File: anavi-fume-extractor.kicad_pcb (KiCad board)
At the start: 2 copper layers, 74.9 x 40.6 mm, 34 parts, among them K1 SANYOU_SRD_Form_C, P1 CONN_01X03, Q1 BC817, U1 I2C_SENS_1, U2 I2C_SENS_1, U3 I2C_SENS_1

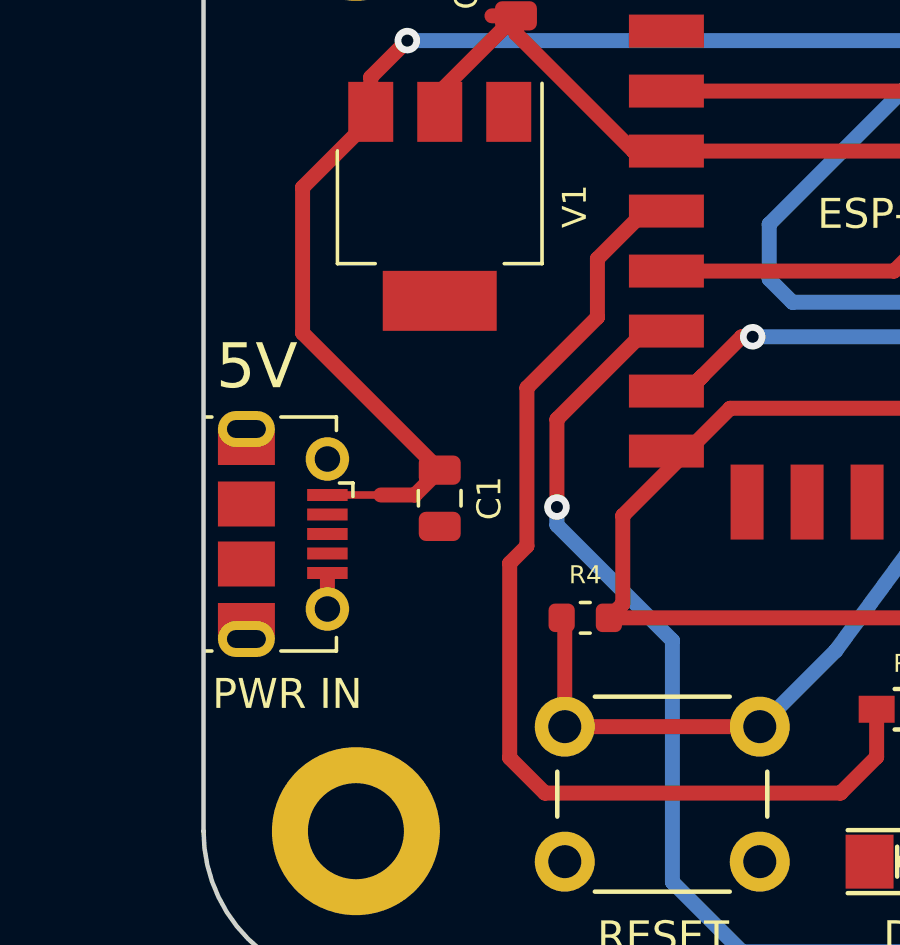
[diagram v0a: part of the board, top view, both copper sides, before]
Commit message: anavi-fume-extractor.kicad_pcb: Move capacitor
Move capacitor C1 to be closer to the microUSB connector.

Suggested-by: Rangel Ivanov <rangelivanov88@gmail.com>
Signed-off-by: Leon Anavi <leon@anavi.org>
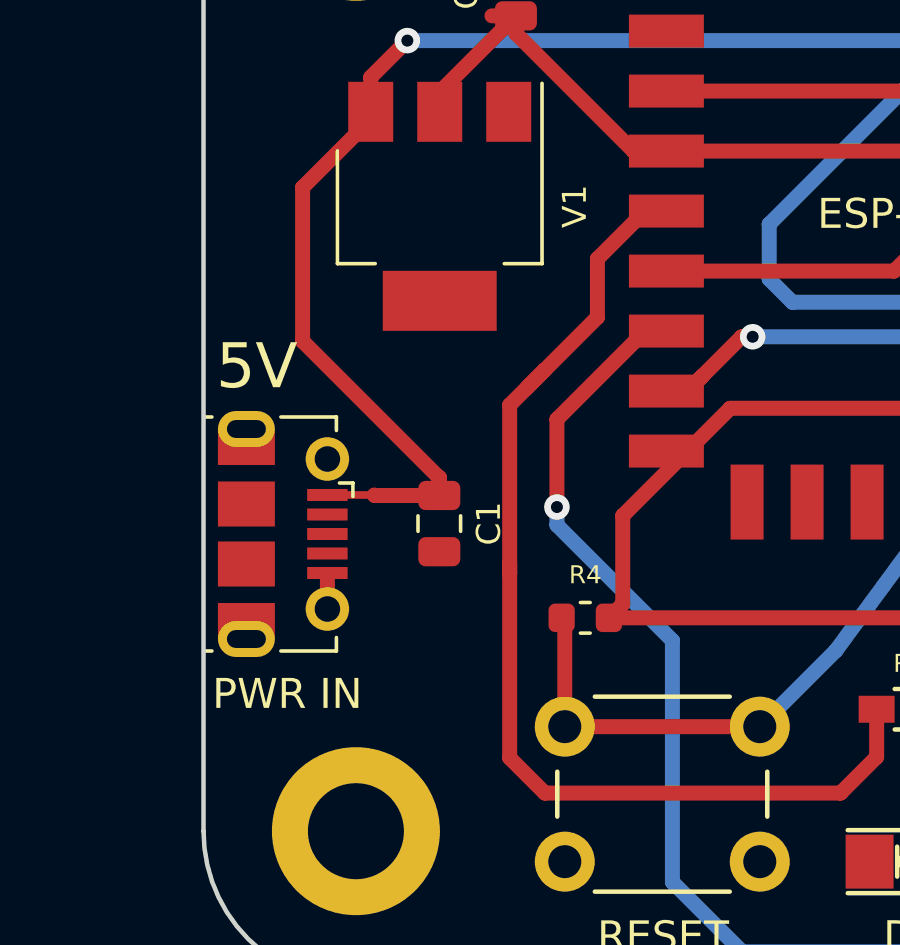
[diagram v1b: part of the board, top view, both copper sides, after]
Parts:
- moved C1 0.85 mm to (72.6, 96.4)
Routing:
- net Net-(ESP-12-Pad4): track 36.3 -> 37.5 mm
- net +5V: track 123.6 -> 124.1 mm
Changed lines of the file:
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@@
     (thickness 1.6)
     (drawings 24)
-    (tracks 235)
+    (tracks 239)
     (zones 0)
     (modules 34)
@@
   )
   (module Capacitor_SMD:C_0805_2012Metric (layer F.Cu)
-    (at 72.644 95.5825 270)
+    (at 72.63 96.4275 270)
     (descr "Capacitor SMD 0805 (2012 Metric), square (rectangular) end terminal, IPC_7351 nominal, (Body size source: https://docs.google.com/spreadsheets/d/1BsfQQcO9C6DZCsRaXUlFlo91Tg2WpOkGARC1WS5S8t0/edit?usp=sharing), generated with kicad-footprint-generator")
     (tags capacitor)
@@
       (effects (font (size 0.8 0.8) (thickness 0.15)))
     )
-    (fp_text value 10uF (at 0 -1.778 270) (layer F.Fab)
+    (fp_text value 10uF (at 2.5625 -0.14) (layer F.Fab)
       (effects (font (size 1 1) (thickness 0.15)))
     )
@@
   (segment (start 86.0044 105.41) (end 76.1492 105.41) (width 0.5) (layer F.Cu) (net 9))
   (segment (start 76.1492 105.41) (end 74.975 104.2358) (width 0.5) (layer F.Cu) (net 9))
-  (segment (start 74.975 104.2358) (end 74.975 97.75) (width 0.5) (layer F.Cu) (net 9))
-  (segment (start 74.975 97.75) (end 75.55 97.175) (width 0.5) (layer F.Cu) (net 9))
-  (segment (start 75.55 91.9) (end 77.9 89.55) (width 0.5) (layer F.Cu) (net 9))
-  (segment (start 75.55 97.175) (end 75.55 91.9) (width 0.5) (layer F.Cu) (net 9))
+  (segment (start 75.55 91.9) (end 76.15 91.3) (width 0.5) (layer F.Cu) (net 9))
+  (segment (start 74.975 98.09) (end 74.975 92.475) (width 0.5) (layer F.Cu) (net 9))
+  (segment (start 74.975 98.09) (end 74.975 97.75) (width 0.5) (layer F.Cu) (net 9))
+  (segment (start 74.975 92.475) (end 76.15 91.3) (width 0.5) (layer F.Cu) (net 9))
+  (segment (start 76.15 91.3) (end 77.9 89.55) (width 0.5) (layer F.Cu) (net 9))
+  (segment (start 74.975 104.2358) (end 74.975 98.09) (width 0.5) (layer F.Cu) (net 9))
   (segment (start 76.812 99.672) (end 76.708 99.568) (width 0.5) (layer F.Cu) (net 10))
   (segment (start 76.812 103.196) (end 76.812 99.672) (width 0.5) (layer F.Cu) (net 10))
@@
   (segment (start 69.3745 95.474) (end 69.4045 95.504) (width 0.254) (layer F.Cu) (net 11))
   (segment (start 68.8995 95.474) (end 69.3745 95.474) (width 0.254) (layer F.Cu) (net 11))
-  (segment (start 71.815 95.474) (end 72.644 94.645) (width 0.5) (layer F.Cu) (net 11))
   (segment (start 70.344 82.952) (end 68.072 85.224) (width 0.5) (layer F.Cu) (net 11))
   (segment (start 70.344 82.702) (end 70.344 82.952) (width 0.5) (layer F.Cu) (net 11))
-  (segment (start 68.072 90.073) (end 72.644 94.645) (width 0.5) (layer F.Cu) (net 11))
-  (segment (start 68.072 85.224) (end 68.072 90.073) (width 0.5) (layer F.Cu) (net 11))
   (segment (start 125.222 73.834) (end 123.651 72.263) (width 0.5) (layer B.Cu) (net 11))
   (segment (start 125.222 75.184) (end 125.222 73.834) (width 0.5) (layer B.Cu) (net 11))
@@
   (segment (start 116.9 82.4) (end 121 82.4) (width 0.5) (layer F.Cu) (net 11))
   (segment (start 114.95 84.35) (end 116.9 82.4) (width 0.5) (layer F.Cu) (net 11))
-  (segment (start 71.815 95.474) (end 70.676 95.474) (width 0.5) (layer F.Cu) (net 11))
-  (segment (start 70.676 95.474) (end 68.8995 95.474) (width 0.254) (layer F.Cu) (net 11))
+  (segment (start 72.63 94.9025) (end 72.64 94.8925) (width 0.5) (layer F.Cu) (net 11))
+  (segment (start 68.072 90.3445) (end 68.072 85.224) (width 0.5) (layer F.Cu) (net 11))
+  (segment (start 72.63 94.9025) (end 68.072 90.3445) (width 0.5) (layer F.Cu) (net 11))
+  (segment (start 72.63 95.49) (end 72.63 94.9025) (width 0.5) (layer F.Cu) (net 11))
+  (segment (start 68.8995 95.474) (end 70.464 95.474) (width 0.254) (layer F.Cu) (net 11))
+  (segment (start 70.48 95.49) (end 72.63 95.49) (width 0.5) (layer F.Cu) (net 11))
+  (segment (start 70.464 95.474) (end 70.48 95.49) (width 0.5) (layer F.Cu) (net 11))
   (segment (start 96.306202 90.01) (end 94.899 90.01) (width 0.5) (layer F.Cu) (net 12))
   (segment (start 94.899 90.01) (end 96.614 90.01) (width 0.5) (layer F.Cu) (net 12))
